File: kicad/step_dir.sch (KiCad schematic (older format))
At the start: 15 parts, among them J1001 tblock2x6, U1001 am26ls32a

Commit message: changed 200mils connector to 150mils 'cause space constraints
I've decided to change 200 mils input connector for encat, rs485 and so
for 150mis 'cose it doesn't deliver so much current and I'd save some
space in the board. I've added the step/dir differential interface that
I've fotgot, and also add differential input to all signals of
incremental encoder interface A/B/I/S .. now lets rock
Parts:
- J1001: footprint Connector_Phoenix_MC:PhoenixContact_MC_1,5_6-G-3.81_1x06_P3.81mm_Horizontal -> servo:tblock02x6_3.81
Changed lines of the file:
@@
 F 0 "J1001" H 8650 4243 39  0000 C CNN
 F 1 "tblock2x6" H 8650 4168 39  0000 C CNN
-F 2 "Connector_Phoenix_MC:PhoenixContact_MC_1,5_6-G-3.81_1x06_P3.81mm_Horizontal" H 8550 4050 50  0001 C CNN
+F 2 "servo:tblock02x6_3.81" H 8550 4050 50  0001 C CNN
 F 3 "../doc/datasheets/tblock2rows.pdf" H 8650 4150 50  0001 C CNN
 	1    8600 3850

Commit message: placing smmall capacitors and resistors nerar his group
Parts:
- U1001: footprint Package_SO:SOIC-16_3.9x9.9mm_P1.27mm -> Package_SO:SOIC-16W_5.3x10.2mm_P1.27mm
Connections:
- net STEP2_A+_H: now reaches J1001.2b (Pin_2b), R1010.2, R1011.1, U1001.14 (A4)
- net STEP2_A-_H: now reaches J1001.3b (Pin_3b), R1011.2, R1012.1, U1001.15 (B4)
- net STEP2_B+_H: now reaches J1001.4b (Pin_4b), R1007.2, R1008.1, U1001.10 (A3)
- net STEP2_B-_H: now reaches J1001.5b (Pin_5b), R1008.2, R1009.1, U1001.9 (B3)
- net QEP1_A+_H renamed STEP1_A+_H
- net STEP1_A+_H: now also U1001.6 (A2); no longer U1001.2 (A1)
- net QEP1_A-_H renamed STEP1_A-_H
- net STEP1_A-_H: now also U1001.7 (B2); no longer U1001.1 (B1)
- net QEP1_B+_H renamed STEP1_B+_H
- net STEP1_B+_H: now also U1001.2 (A1); no longer U1001.6 (A2)
- net QEP1_B-_H renamed STEP1_B-_H
- net STEP1_B-_H: now also U1001.1 (B1); no longer U1001.7 (B2)
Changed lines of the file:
@@
 $EndComp
 Text Label 8150 3750 0    20   ~ 0
-QEP1_A+_H
+STEP1_A+_H
 Text Label 8150 3850 0    20   ~ 0
-QEP1_A-_H
+STEP1_A-_H
 Text Label 8150 3950 0    20   ~ 0
-QEP1_B+_H
+STEP1_B+_H
 Text Label 8150 4050 0    20   ~ 0
-QEP1_B-_H
+STEP1_B-_H
 Wire Wire Line
 	7000 3200 7000 3850
@@
 	8650 4250 9000 4250
 $Comp
-L servo:am26ls32a U?
+L servo:am26ls32a U1001
 U 1 1 6322E22C
 P 8950 5750
-AR Path="/5E092156/6322E22C" Ref="U?"  Part="1"
+AR Path="/5E092156/6322E22C" Ref="U1001"  Part="1"
 AR Path="/5DE3DF56/6322E22C" Ref="U1001"  Part="1"
 F 0 "U1001" H 8800 6800 39  0000 C CNN
 F 1 "am26ls32a" H 8750 6700 39  0000 C CNN
-F 2 "Package_SO:SOIC-16_3.9x9.9mm_P1.27mm" H 9950 4800 50  0001 C CNN
+F 2 "Package_SO:SOIC-16W_5.3x10.2mm_P1.27mm" H 9950 4800 50  0001 C CNN
 F 3 "../doc/datasheets/am26ls32a.pdf" H 8950 5350 50  0001 C CNN
 	1    8950 5750
@@
 	7800 5750 7800 5250
 Wire Wire Line
-	8200 5350 8200 4800
-Wire Wire Line
-	8200 4800 6900 4800
-Wire Wire Line
 	6900 4800 6900 3750
 Connection ~ 6900 3750
 Wire Wire Line
 	7000 3850 7000 4700
-Wire Wire Line
-	7000 4700 8300 4700
-Wire Wire Line
-	8300 4700 8300 5350
 Connection ~ 7000 3850
-Wire Wire Line
-	8400 5350 8400 4600
-Wire Wire Line
-	8400 4600 7300 4600
 Wire Wire Line
 	7300 3000 7300 3950
@@
 	7400 4050 7400 4500
 Wire Wire Line
-	7400 4500 8500 4500
-Wire Wire Line
-	8500 4500 8500 5350
+	7400 4500 8300 4500
 Connection ~ 7400 4050
 Wire Wire Line
@@
 Text Notes 8400 1350 0    20   ~ 0
 The isolation part is shared with QEP
+Wire Wire Line
+	8500 4700 8500 5350
+Wire Wire Line
+	7000 4700 8500 4700
+Wire Wire Line
+	8400 4800 8400 5350
+Wire Wire Line
+	6900 4800 8400 4800
+Wire Wire Line
+	8300 5350 8300 4500
+Wire Wire Line
+	8200 5350 8200 4600
+Wire Wire Line
+	8200 4600 7300 4600
+Text Label 8950 3750 0    20   ~ 0
+STEP2_A+_H
+Text Label 8950 3850 0    20   ~ 0
+STEP2_A-_H
+Text Label 8950 3950 0    20   ~ 0
+STEP2_B+_H
+Text Label 8950 4050 0    20   ~ 0
+STEP2_B-_H
 $EndSCHEMATC

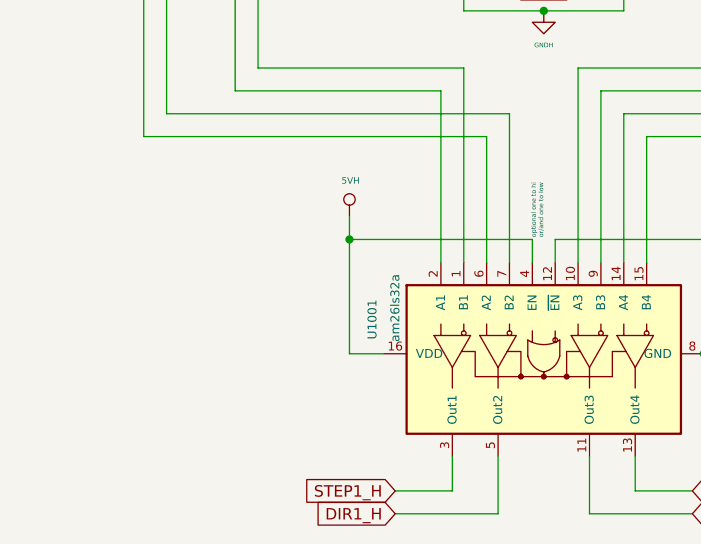
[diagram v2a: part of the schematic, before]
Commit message: All IC placed inside board size but....
I've placed all stuff on board size even thought all are in groups I've
to move the IC to route them. Let's begin
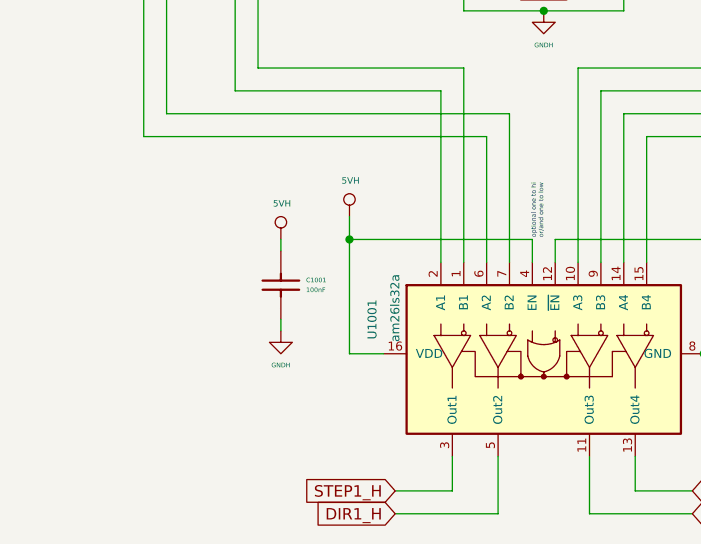
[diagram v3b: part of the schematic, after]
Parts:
- added C1001: 100nF, servo:C_0603_1608Metric, symbol servo:Capacitor
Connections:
- net 5VH: now also C1001.2 (Capacitor)
- net GNDH: now also C1001.1
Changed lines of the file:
@@
 Text Label 8950 4050 0    20   ~ 0
 STEP2_B-_H
+Wire Wire Line
+	7500 5600 7500 5650
+Wire Wire Line
+	7500 5300 7500 5250
+$Comp
+L servo:Capacitor C?
+U 1 1 5F04EFB4
+P 7500 5400
+AR Path="/605B70F2/5F04EFB4" Ref="C?"  Part="1"
+AR Path="/5E092156/5F04EFB4" Ref="C?"  Part="1"
+AR Path="/5DE3DF56/5F04EFB4" Ref="C1001"  Part="1"
+F 0 "C1001" V 7528 5510 20  0000 L CNN
+F 1 "100nF" V 7571 5510 20  0000 L CNN
+F 2 "servo:C_0603_1608Metric" H 7500 5300 60  0001 C CNN
+F 3 "" H 7500 5400 60  0000 C CNN
+	1    7500 5400
+	0    1    1    0
+$EndComp
+$Comp
+L servo:5VH #PWR?
+U 1 1 5F04EFBB
+P 7500 5250
+AR Path="/5DE49152/5F04EFBB" Ref="#PWR?"  Part="1"
+AR Path="/5E1BAEAA/5F04EFBB" Ref="#PWR?"  Part="1"
+AR Path="/5DE3DF56/5F04EFBB" Ref="#PWR0259"  Part="1"
+AR Path="/5E092156/5F04EFBB" Ref="#PWR?"  Part="1"
+F 0 "#PWR0259" H 7500 5050 20  0001 C CNN
+F 1 "5VH" H 7505 5407 28  0000 C CNN
+F 2 "" H 7500 5250 50  0001 C CNN
+F 3 "" H 7500 5250 50  0001 C CNN
+	1    7500 5250
+	1    0    0    -1
+$EndComp
+$Comp
+L servo:GNDH #PWR?
+U 1 1 5F04EFC1
+P 7500 5650
+AR Path="/5DDE8C5E/5F04EFC1" Ref="#PWR?"  Part="1"
+AR Path="/5E092156/5F04EFC1" Ref="#PWR?"  Part="1"
+AR Path="/5DE3DF56/5F04EFC1" Ref="#PWR0260"  Part="1"
+F 0 "#PWR0260" H 7500 5400 30  0001 C CNN
+F 1 "GNDH" H 7500 5500 20  0000 C CNN
+F 2 "" H 7500 5650 50  0001 C CNN
+F 3 "" H 7500 5650 50  0001 C CNN
+	1    7500 5650
+	1    0    0    -1
+$EndComp
 $EndSCHEMATC

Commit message: touting....
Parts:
- added JP1002: jumper, Jumper:SolderJumper-3_P1.3mm_Open_RoundedPad1.0x1.5mm, symbol servo:Jumper_3_Bridged12
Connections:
- net GNDH: now also JP1002.3 (B); no longer J1001.6a (Pin_6a), J1001.6b (Pin_6b)
- new net: J1001.6a (Pin_6a), J1001.6b (Pin_6b), JP1002.2 (C)
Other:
- moved on the sheet: C1001, U1001

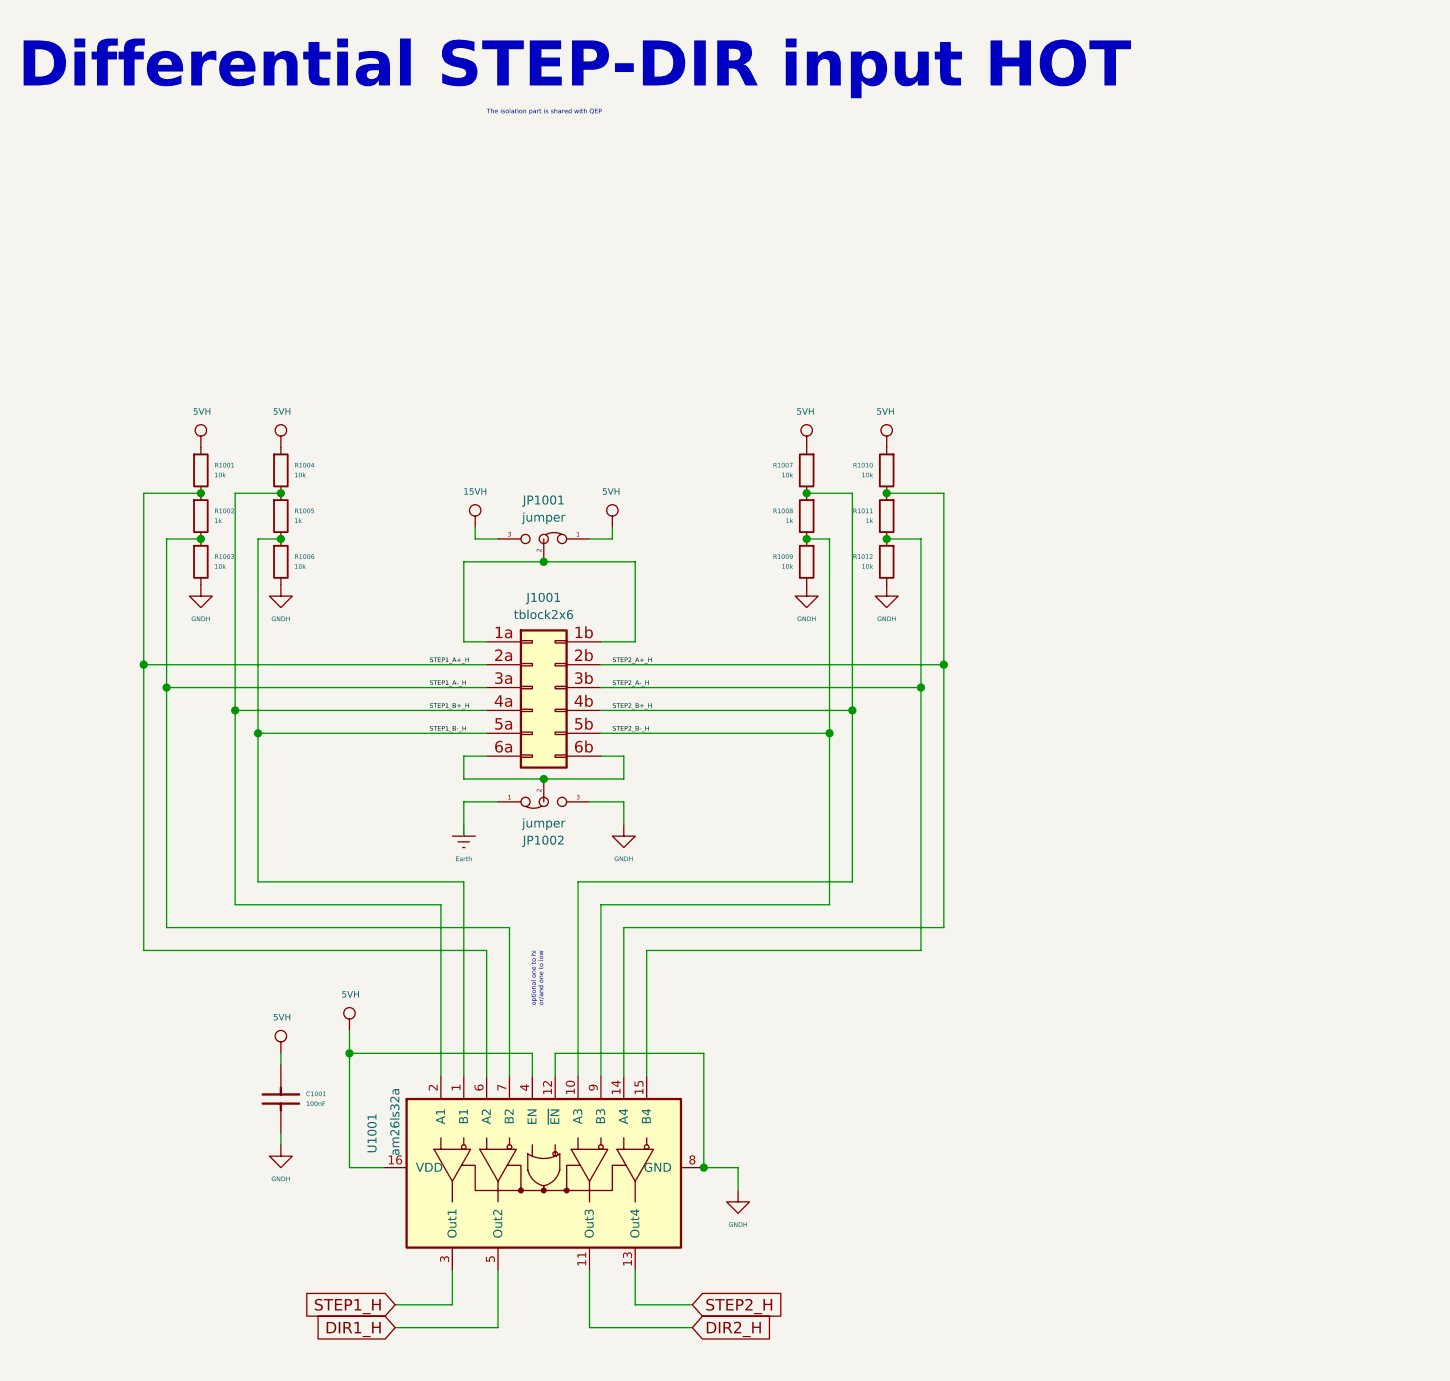
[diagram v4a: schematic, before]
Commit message: moving ethernet connector to right and depopulate 15vh
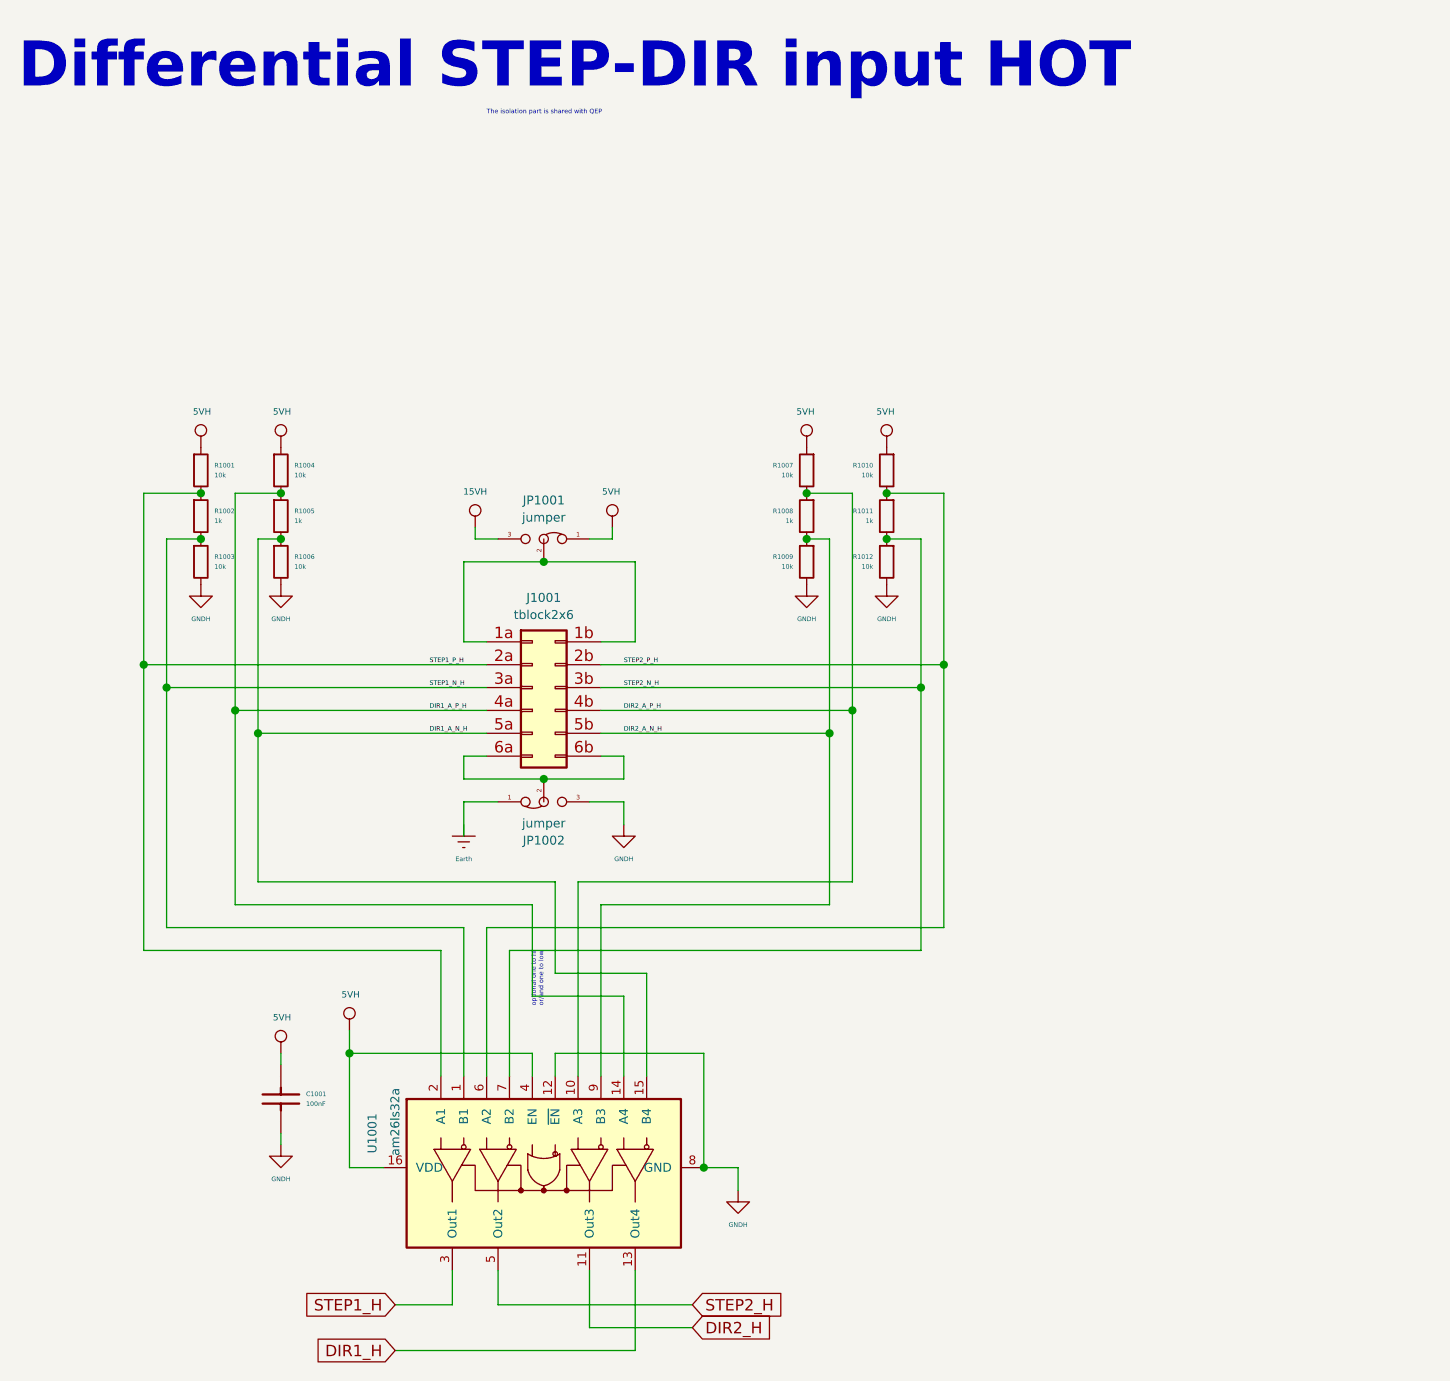
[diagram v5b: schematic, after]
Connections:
- net DIR1_H: now also U1001.13 (Out4); no longer U1001.5 (Out2)
- net STEP2_H: now also U1001.5 (Out2); no longer U1001.13 (Out4)
- net STEP1_A+_H renamed STEP1_P_H
- net STEP1_P_H: now also U1001.2 (A1); no longer U1001.6 (A2)
- net STEP1_A-_H renamed STEP1_N_H
- net STEP1_N_H: now also U1001.1 (B1); no longer U1001.7 (B2)
- net STEP1_B+_H renamed DIR1_A_P_H
- net DIR1_A_P_H: now also U1001.14 (A4); no longer U1001.2 (A1)
- net STEP1_B-_H renamed DIR1_A_N_H
- net DIR1_A_N_H: now also U1001.15 (B4); no longer U1001.1 (B1)
- net STEP2_A+_H renamed STEP2_P_H
- net STEP2_P_H: now also U1001.6 (A2); no longer U1001.14 (A4)
- net STEP2_A-_H renamed STEP2_N_H
- net STEP2_N_H: now also U1001.7 (B2); no longer U1001.15 (B4)
- net STEP2_B+_H renamed DIR2_A_P_H
- net STEP2_B-_H renamed DIR2_A_N_H
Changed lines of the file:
@@
 	1    0    0    -1
 $EndComp
+Text Label 8150 3950 0    20   ~ 0
+DIR1_A_P_H
 Text Label 8150 3750 0    20   ~ 0
-STEP1_A+_H
+STEP1_P_H
 Text Label 8150 3850 0    20   ~ 0
-STEP1_A-_H
-Text Label 8150 3950 0    20   ~ 0
-STEP1_B+_H
-Text Label 8150 4050 0    20   ~ 0
-STEP1_B-_H
+STEP1_N_H
 Wire Wire Line
 	7000 3200 7000 3850
@@
 Wire Wire Line
 	7400 4050 7400 4700
-Wire Wire Line
-	7400 4700 8300 4700
 Connection ~ 7400 4050
 Wire Wire Line
@@
 	8900 4800 8900 5550
 Wire Wire Line
-	9000 5550 9000 4900
-Wire Wire Line
-	9000 4900 10400 4900
-Wire Wire Line
 	10400 3750 10400 4900
-Wire Wire Line
-	10300 5000 9100 5000
-Wire Wire Line
-	9100 5000 9100 5550
 Wire Wire Line
 	10300 3850 10300 5000
@@
 	8250 6550 8250 6400
 Wire Wire Line
-	8450 6400 8450 6650
-Wire Wire Line
 	8850 6650 8850 6400
-Wire Wire Line
-	9050 6400 9050 6550
 Text GLabel 8000 6550 0    50   Input ~ 0
 STEP1_H
-Text GLabel 8000 6650 0    50   Input ~ 0
+Text GLabel 8000 6750 0    50   Input ~ 0
 DIR1_H
 Wire Wire Line
 	8250 6550 8000 6550
-Wire Wire Line
-	8000 6650 8450 6650
 Text GLabel 9300 6550 2    50   Input ~ 0
 STEP2_H
@@
 DIR2_H
 Wire Wire Line
-	9300 6550 9050 6550
-Wire Wire Line
 	8850 6650 9300 6650
 Text Notes 8400 1350 0    20   ~ 0
 The isolation part is shared with QEP
-Wire Wire Line
-	8500 4900 8500 5550
-Wire Wire Line
-	7000 4900 8500 4900
-Wire Wire Line
-	8400 5000 8400 5550
-Wire Wire Line
-	6900 5000 8400 5000
-Wire Wire Line
-	8300 5550 8300 4700
-Wire Wire Line
-	8200 5550 8200 4800
-Wire Wire Line
-	8200 4800 7300 4800
-Text Label 8950 3750 0    20   ~ 0
-STEP2_A+_H
-Text Label 8950 3850 0    20   ~ 0
-STEP2_A-_H
-Text Label 8950 3950 0    20   ~ 0
-STEP2_B+_H
-Text Label 8950 4050 0    20   ~ 0
-STEP2_B-_H
 Wire Wire Line
 	7500 5800 7500 5850
@@
 	8650 4250 9000 4250
 Connection ~ 8650 4250
+Text Label 8150 4050 0    20   ~ 0
+DIR1_A_N_H
+Text Label 9000 3950 0    20   ~ 0
+DIR2_A_P_H
+Text Label 9000 4050 0    20   ~ 0
+DIR2_A_N_H
+Text Label 9000 3750 0    20   ~ 0
+STEP2_P_H
+Text Label 9000 3850 0    20   ~ 0
+STEP2_N_H
+Wire Wire Line
+	8300 5550 8300 4900
+Wire Wire Line
+	8300 4900 7000 4900
+Wire Wire Line
+	6900 5000 8200 5000
+Wire Wire Line
+	8200 5000 8200 5550
+Wire Wire Line
+	9050 6750 9050 6400
+Wire Wire Line
+	8000 6750 9050 6750
+Wire Wire Line
+	8450 6400 8450 6550
+Wire Wire Line
+	8450 6550 9300 6550
+Wire Wire Line
+	8400 4900 8400 5550
+Wire Wire Line
+	8400 4900 10400 4900
+Wire Wire Line
+	8500 5550 8500 5000
+Wire Wire Line
+	8500 5000 10300 5000
+Wire Wire Line
+	8600 4800 8600 5200
+Wire Wire Line
+	8600 5200 9000 5200
+Wire Wire Line
+	9000 5200 9000 5550
+Wire Wire Line
+	7300 4800 8600 4800
+Wire Wire Line
+	8700 4700 8700 5100
+Wire Wire Line
+	8700 5100 9100 5100
+Wire Wire Line
+	9100 5100 9100 5550
+Wire Wire Line
+	7400 4700 8700 4700
 $EndSCHEMATC
